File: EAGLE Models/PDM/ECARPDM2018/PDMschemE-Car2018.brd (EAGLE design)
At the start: 85.1 x 102.9 mm, 45 parts, among them Q1 MPSA56, Q2 MPSA56, Q3 MPSA56, Q4 MPSA56, Q5 MPSA56, Q6 MPSA56, Q7 IRF40B207, X1 A30605-ND, X2 HARWIN_M20-9980445

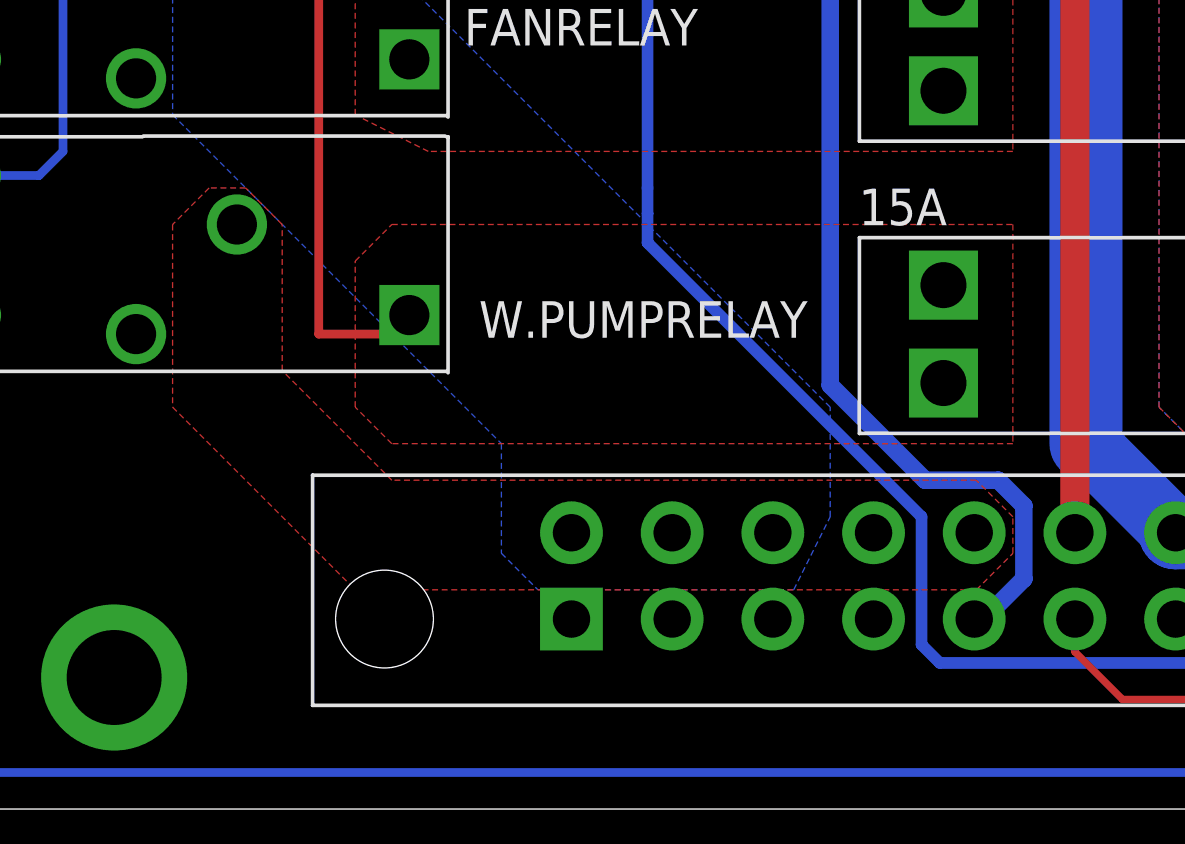
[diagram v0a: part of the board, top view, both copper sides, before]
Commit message: rerouted pump out to pins 1 and 2 from 17 and 18
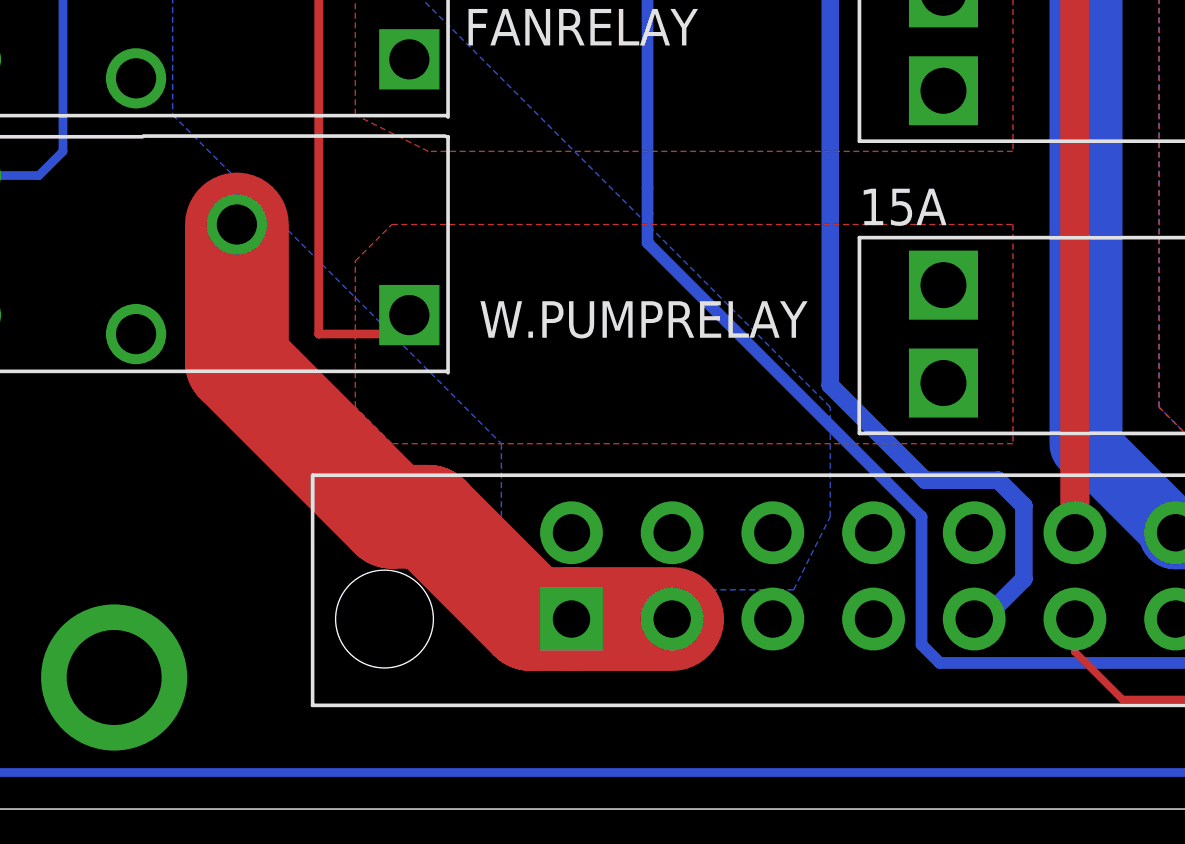
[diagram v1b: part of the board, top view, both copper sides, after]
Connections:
- net W.PUMP: now also U$4.P$1, U$4.P$2; no longer U$4.P$17, U$4.P$18
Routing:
- net W.PUMP: track 0.00 -> 23.6 mm
- removed copper zone on layer 1, net W.PUMP
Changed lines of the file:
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@@
 <?xml version="1.0" encoding="utf-8"?>
 <!DOCTYPE eagle SYSTEM "eagle.dtd">
-<eagle version="8.4.1">
+<eagle version="8.3.1">
 <drawing>
 <settings>
@@
 <param name="dpMaxLengthDifference" value="10mm"/>
 <param name="dpGapFactor" value="2.5"/>
+<param name="checkGrid" value="0"/>
 <param name="checkAngle" value="0"/>
 <param name="checkFont" value="1"/>
 <param name="checkRestrict" value="1"/>
-<param name="checkStop" value="0"/>
 <param name="useDiameter" value="13"/>
 <param name="maxErrors" value="50"/>
@@
 <signal name="W.PUMP">
 <contactref element="W.PUMPRELAY" pad="NO"/>
-<contactref element="U$4" pad="P$17"/>
-<contactref element="U$4" pad="P$18"/>
-<polygon width="0.1524" layer="1" thermals="no">
-<vertex x="11.43" y="21.59"/>
-<vertex x="10.16" y="20.32"/>
-<vertex x="10.16" y="13.97"/>
-<vertex x="16.51" y="7.62"/>
-<vertex x="38.1" y="7.62"/>
-<vertex x="39.37" y="8.89"/>
-<vertex x="39.37" y="10.16"/>
-<vertex x="38.1" y="11.43"/>
-<vertex x="17.78" y="11.43"/>
-<vertex x="13.97" y="15.24"/>
-<vertex x="13.97" y="20.32"/>
-<vertex x="12.7" y="21.59"/>
-</polygon>
+<contactref element="U$4" pad="P$1"/>
+<contactref element="U$4" pad="P$2"/>
+<wire x1="12.3952" y1="20.32" x2="12.3952" y2="15.5448" width="3.6068" layer="1"/>
+<wire x1="12.3952" y1="15.5448" x2="17.78" y2="10.16" width="3.6068" layer="1"/>
+<wire x1="17.78" y1="10.16" x2="19.05" y2="10.16" width="3.6068" layer="1"/>
+<wire x1="22.606" y1="6.604" x2="24.026" y2="6.604" width="3.6068" layer="1"/>
+<wire x1="19.05" y1="10.16" x2="22.606" y2="6.604" width="3.6068" layer="1"/>
+<wire x1="24.026" y1="6.604" x2="27.526" y2="6.604" width="3.6068" layer="1"/>
 </signal>
 <signal name="GND">
